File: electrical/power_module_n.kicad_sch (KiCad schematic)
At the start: 16 parts, among them J1 Power connector for bulb driv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, J2 Need to cut return bulb wiring, J3 Ground connector from bulb wi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, Q2 BC548B, Q5 IFRZ44N

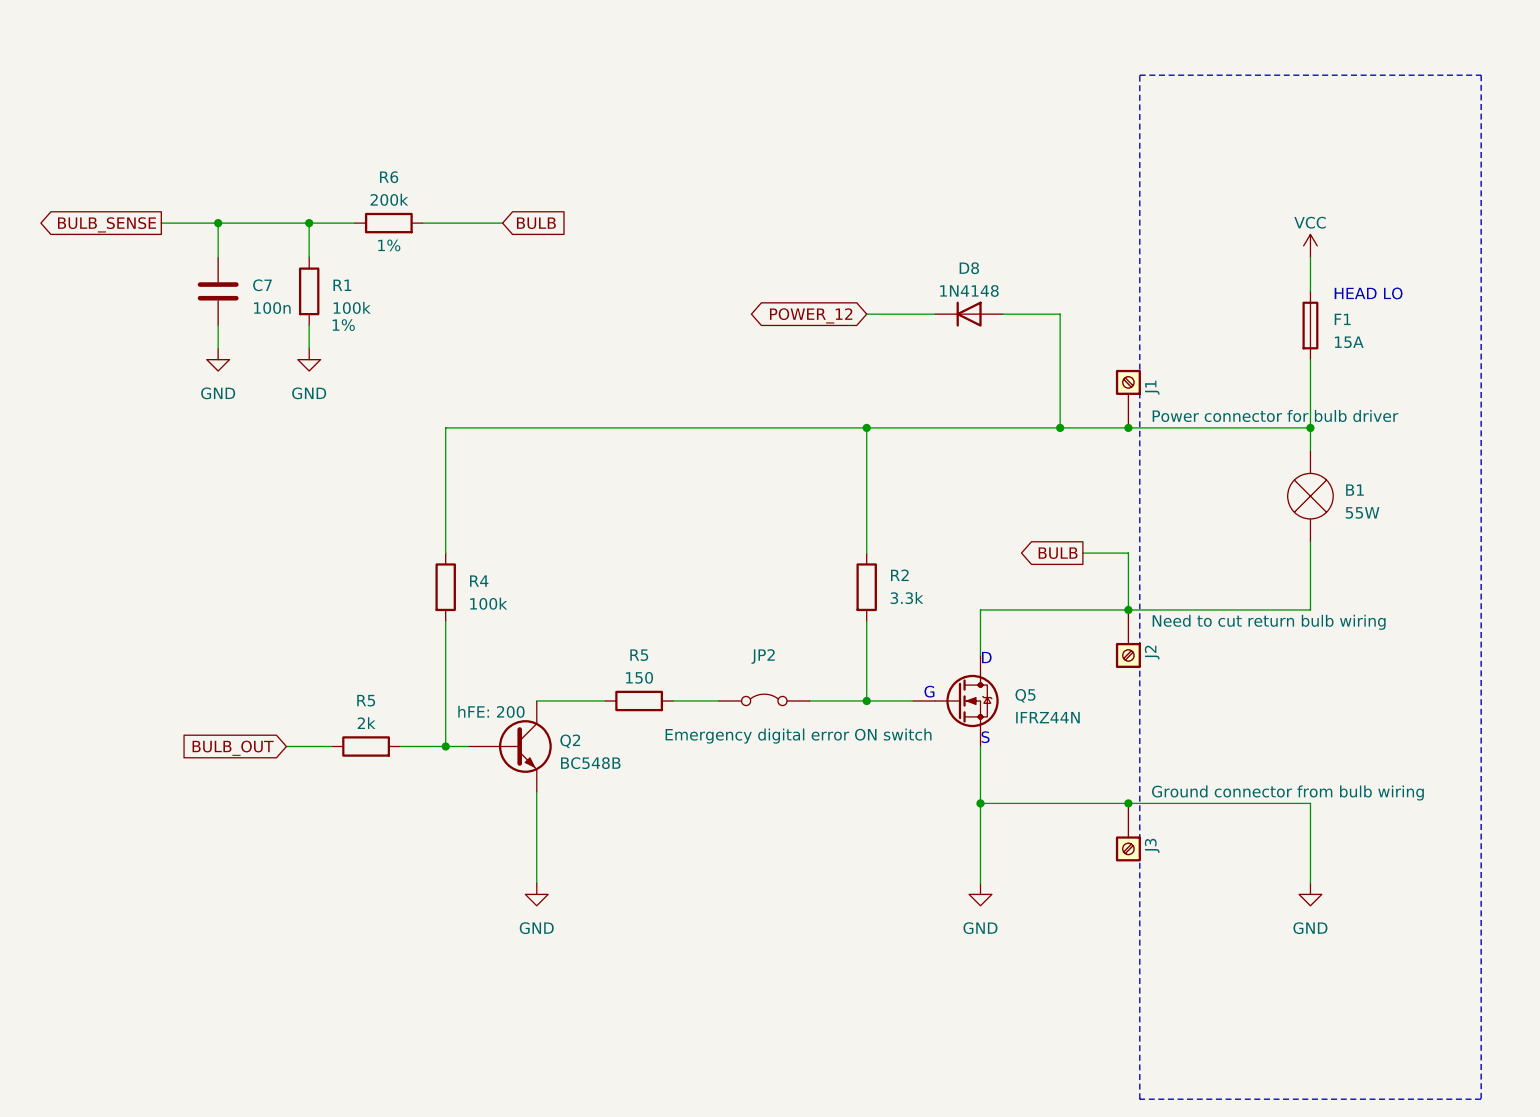
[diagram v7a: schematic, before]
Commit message: Aktualizacja KiCad i schematu - LED do debugowania
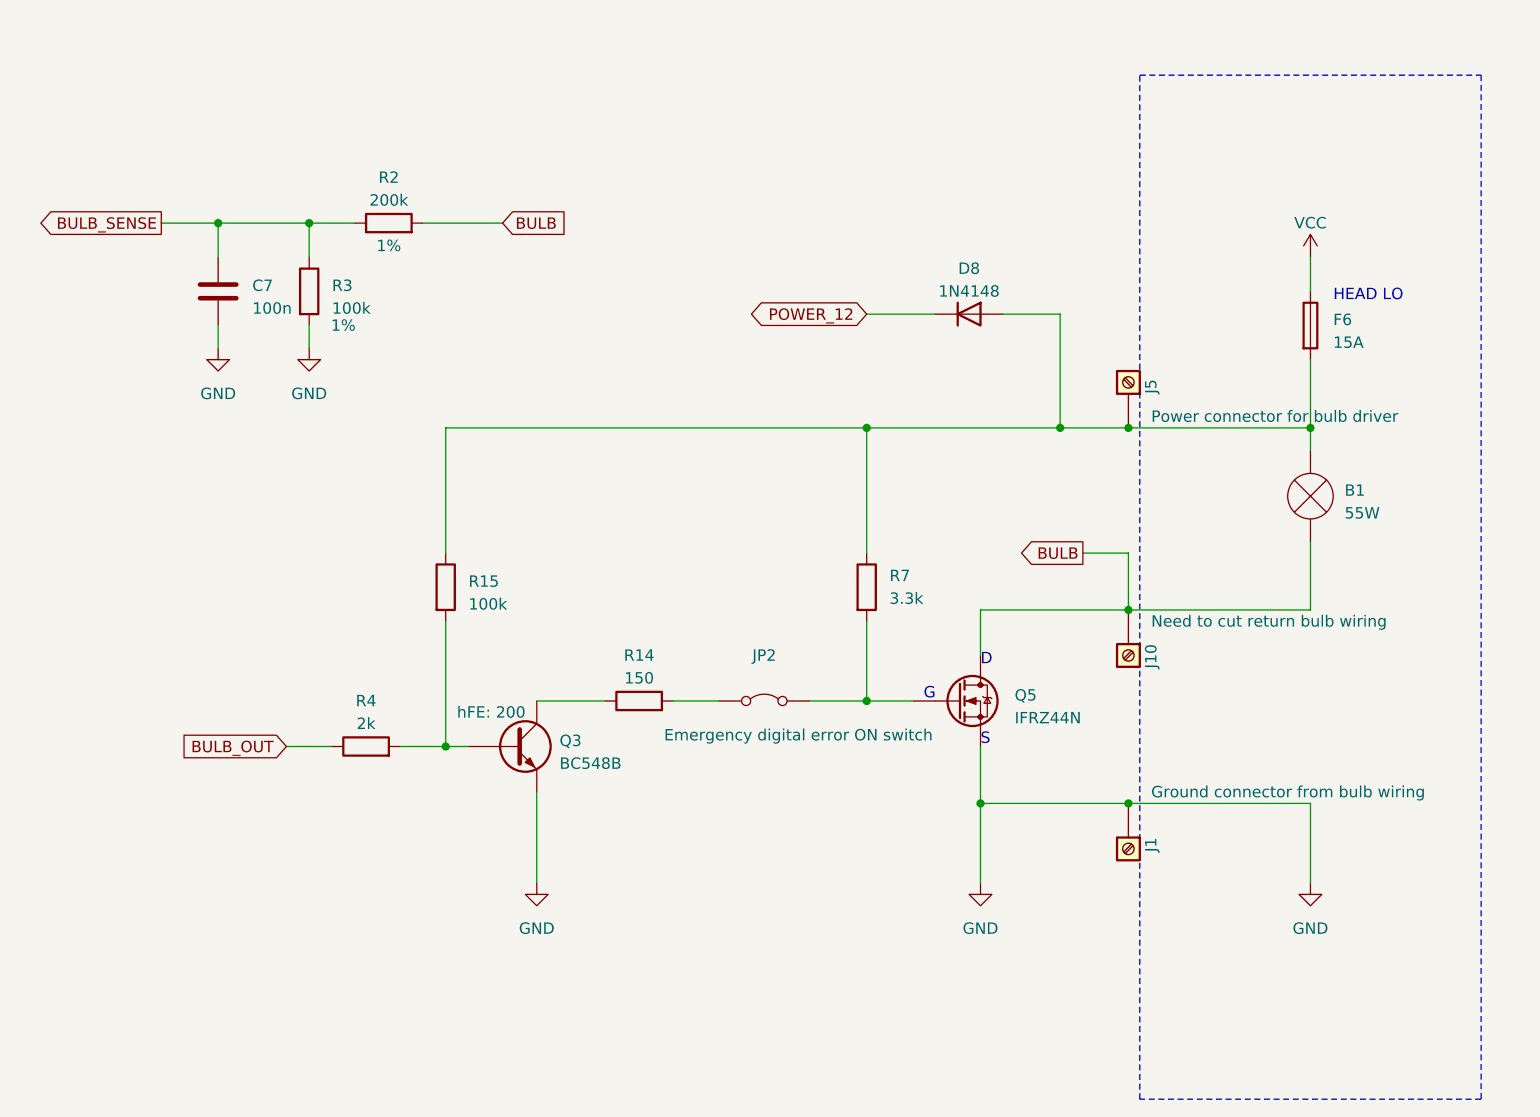
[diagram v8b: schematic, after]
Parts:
- renumbered F1 to F6, J3 to J1, J2 to J10, J1 to J5, Q2 to Q3, R5 to R14, R4 to R15, R6 to R2, R1 to R3, R5 to R4, R2 to R7
